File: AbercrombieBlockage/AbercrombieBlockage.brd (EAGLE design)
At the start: 54 x 52 mm, 29 parts, among them U1 CY8CKIT-142, U2 DMN3135LVT, U3 DMN3135LVT, U4 DMN3135LVT, U5 M95M01, U6 LDK130M-R

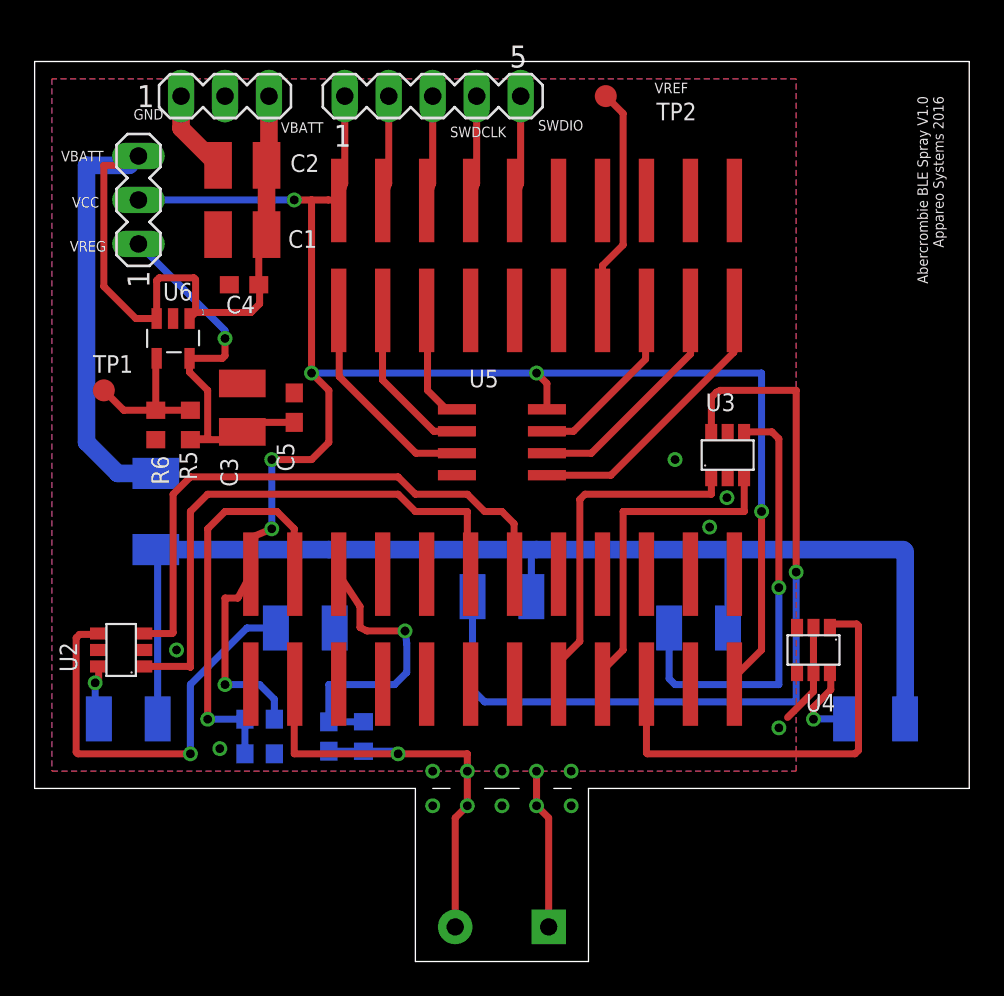
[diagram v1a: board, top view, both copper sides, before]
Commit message: Updated to fix issues with the layout.
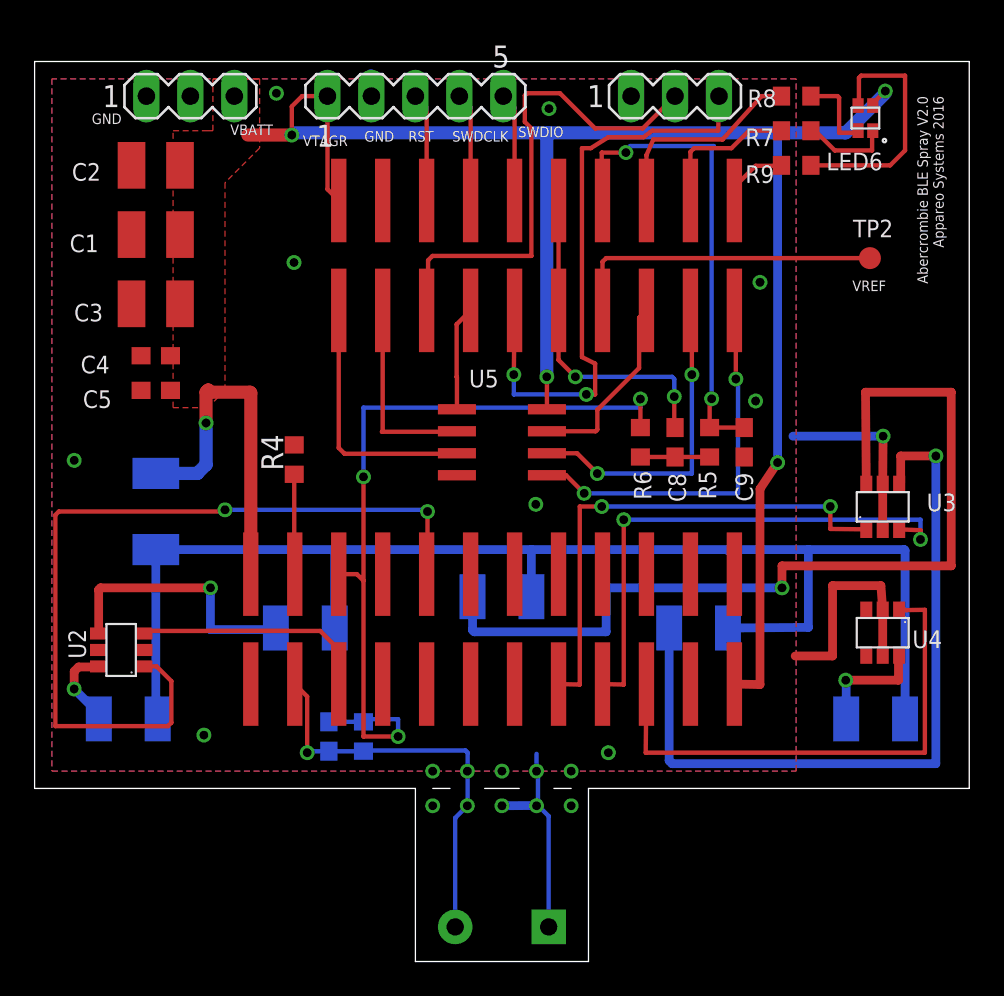
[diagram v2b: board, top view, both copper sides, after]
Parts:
- removed R3: DNP, resistor:R0603
- removed TP1: TPB1,27, testpad:B1,27
- removed U6: LDK130M-R, NicksParts:SOT23-5
- added C8: 20n, resistor:C0603
- added C9: 10n, resistor:C0603
- added LED6: LTST-C19HE1WT, NicksParts:LTST-C19HE1WT
- added R7: 200, resistor:R0603
- added R8, R9: 60, resistor:R0603
- R5, R6: value DNP -> 937.82k
- moved SV2 31.6 mm to (37.0, 50.0), turned to 0 degrees
- moved R5 30.0 mm to (39.0, 30.0)
- moved R6 28.0 mm to (35.0, 30.0)
- moved TP2 17.9 mm to (48.3, 40.6)
- moved R4 17.1 mm to (15.0, 29.0), flipped to the top, turned to 90 degrees
- moved U3 9.45 mm to (49.0, 26.3)
- moved C5 8.06 mm to (7.00, 33.0), turned to 180 degrees
- moved C3 7.81 mm to (7.00, 38.0), turned to 180 degrees
- moved C4 6.54 mm to (7.00, 35.0)
- moved C1 5.00 mm to (7.00, 42.0)
- moved C2 5.00 mm to (7.00, 46.0)
- moved U4 4.12 mm to (49.0, 19.0)
- moved SV1 2.00 mm to (9.00, 50.0)
- moved SV3 1.00 mm to (22.0, 50.0)
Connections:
- removed net VBATT: C1.1, C2.1, C4.1, R1.2, SV1.3, SV2.3, U6.1, U6.3
- new net BLUE: R9.2, U1.0.1
- new net GREEN: R8.2, U1.0.5
- new net N$11: LED6.GREEN, R8.1
- new net N$13: LED6.BLUE, R9.1
- new net OPAMP2+: C9.2, R5.2, U1.1
- new net OPAMP2_OUT: C8.1, U1.1.1, U1.1.2
- new net RED: R7.2, U1.0.3
- new net UART_RX: SV2.3, U1.1.4
- new net UART_TX: SV2.2, U1.1.5
- net CS: now also U1.1.3; no longer U1.1.5
- net GND: now also C9.1, SV2.1; no longer R6.2, U6.2
- net LED1: now also U1.2.6; no longer U1.4.1
- net LED2: now also U1.2.3; no longer U1.4.0
- net N$10: now also LED6.RED, R7.1; no longer R5.2, R6.1, TP1.TP, U6.4
- net N$7: now also C8.2, R6.2; no longer C3.1, C5.1, SV2.1, U6.5
- net OPAMP+: no longer R3.2
- net OPAMP_OUT: now also R6.1
- net VCC: now also C1.1, C2.1, C3.1, C4.1, C5.1, LED6.A, R1.2, SV1.3; no longer R3.1, SV2.2
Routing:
- net VBATT: track 60.1 -> 0.00 mm
- net UART_RX: track 0.00 -> 34.6 mm, vias 0 -> 2
- net UART_TX: track 0.00 -> 28.8 mm
- net OPAMP_OUT: track 17.4 -> 45.8 mm, vias 1 -> 3
- net OPAMP2+: track 0.00 -> 27.8 mm, vias 0 -> 2
- net LED2: track 35.1 -> 13.8 mm
- net OPAMP2_OUT: track 0.00 -> 19.2 mm, vias 0 -> 2
- net N$7: track 23.2 -> 4.00 mm, vias 1 -> 0
- net OPAMP+: track 24.8 -> 5.78 mm, vias 1 -> 0
- net N$5: track 25.8 -> 44.6 mm
- net VCC: track 101.8 -> 119.7 mm, vias 7 -> 5
- net LED1: track 33.1 -> 48.6 mm, vias 0 -> 2
- net N$13: track 0.00 -> 14.5 mm
- net GREEN: track 0.00 -> 12.1 mm
- net LED4: track 19.4 -> 30.8 mm, vias 0 -> 2
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- added copper zone on layer 1, net VCC
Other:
- board text added: "Abercrombie BLE Spray V2.0 Appareo Systems 2016"
- board text added: "RST"
- board text added: "VTAGR"
- board text removed: "Abercrombie BLE Spray V1.0 Appareo Systems 2016"
- board text removed: "VCC"
- board text removed: "VREG"

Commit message: Updated Abercrombie values.
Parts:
- C1: value 100u -> 220u
- C2: value 1u -> 220u
- C8: value 20n -> 0
- C9: value 10n -> 620K
- R5: value 937.82k -> 1M
- R6: value 937.82k -> DNP
- R7: value 200 -> 360
- R8, R9: value 60 -> 360
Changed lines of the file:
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@@
 <grid distance="0.05" unitdist="inch" unit="inch" style="lines" multiple="1" display="yes" altdistance="0.005" altunitdist="inch" altunit="inch"/>
 <layers>
-<layer number="1" name="Top" color="4" fill="1" visible="yes" active="yes"/>
+<layer number="1" name="Top" color="4" fill="1" visible="no" active="yes"/>
 <layer number="16" name="Bottom" color="1" fill="1" visible="yes" active="yes"/>
-<layer number="17" name="Pads" color="2" fill="1" visible="yes" active="yes"/>
-<layer number="18" name="Vias" color="2" fill="1" visible="yes" active="yes"/>
-<layer number="19" name="Unrouted" color="6" fill="1" visible="yes" active="yes"/>
-<layer number="20" name="Dimension" color="15" fill="1" visible="yes" active="yes"/>
-<layer number="21" name="tPlace" color="16" fill="1" visible="yes" active="yes"/>
-<layer number="22" name="bPlace" color="14" fill="1" visible="yes" active="yes"/>
-<layer number="23" name="tOrigins" color="15" fill="1" visible="yes" active="yes"/>
-<layer number="24" name="bOrigins" color="15" fill="1" visible="yes" active="yes"/>
+<layer number="17" name="Pads" color="2" fill="1" visible="no" active="yes"/>
+<layer number="18" name="Vias" color="2" fill="1" visible="no" active="yes"/>
+<layer number="19" name="Unrouted" color="6" fill="1" visible="no" active="yes"/>
+<layer number="20" name="Dimension" color="15" fill="1" visible="no" active="yes"/>
+<layer number="21" name="tPlace" color="16" fill="1" visible="no" active="yes"/>
+<layer number="22" name="bPlace" color="14" fill="1" visible="no" active="yes"/>
+<layer number="23" name="tOrigins" color="15" fill="1" visible="no" active="yes"/>
+<layer number="24" name="bOrigins" color="15" fill="1" visible="no" active="yes"/>
 <layer number="25" name="tNames" color="7" fill="1" visible="no" active="yes"/>
 <layer number="26" name="bNames" color="7" fill="1" visible="no" active="yes"/>
@@
 <layer number="43" name="vRestrict" color="2" fill="10" visible="no" active="yes"/>
 <layer number="44" name="Drills" color="7" fill="1" visible="no" active="yes"/>
-<layer number="45" name="Holes" color="7" fill="1" visible="yes" active="yes"/>
+<layer number="45" name="Holes" color="7" fill="1" visible="no" active="yes"/>
 <layer number="46" name="Milling" color="3" fill="1" visible="no" active="yes"/>
 <layer number="47" name="Measures" color="7" fill="1" visible="no" active="yes"/>
 <layer number="48" name="Document" color="7" fill="1" visible="no" active="yes"/>
 <layer number="49" name="Reference" color="7" fill="1" visible="no" active="yes"/>
-<layer number="51" name="tDocu" color="6" fill="1" visible="yes" active="yes"/>
+<layer number="51" name="tDocu" color="6" fill="1" visible="no" active="yes"/>
 <layer number="52" name="bDocu" color="7" fill="1" visible="no" active="yes"/>
 <layer number="90" name="Modules" color="5" fill="1" visible="no" active="no"/>
@@
 </autorouter>
 <elements>
-<element name="C1" library="resistor" package="C1210" value="100u" x="7" y="42" smashed="yes" rot="R180">
+<element name="C1" library="resistor" package="C1210" value="220u" x="7" y="42" smashed="yes" rot="R180">
 <attribute name="NAME" x="3.698" y="42" size="1.016" layer="25" rot="R180"/>
 <attribute name="VALUE" x="9.905" y="39.175" size="1.27" layer="27" rot="R180"/>
 </element>
-<element name="C2" library="resistor" package="C1210" value="1u" x="7" y="46" smashed="yes" rot="R180">
+<element name="C2" library="resistor" package="C1210" value="220u" x="7" y="46" smashed="yes" rot="R180">
 <attribute name="NAME" x="3.825" y="46.127" size="1.016" layer="25" rot="R180"/>
 <attribute name="VALUE" x="8.905" y="49.175" size="1.27" layer="27" rot="R180"/>
@@
 <attribute name="NAME" x="49" y="46.73" size="1.016" layer="25" rot="R180"/>
 </element>
-<element name="C8" library="resistor" package="C0603" value="20n" x="37" y="30" smashed="yes" rot="R270">
+<element name="C8" library="resistor" package="C0603" value="0" x="37" y="30" smashed="yes" rot="R270">
 <attribute name="NAME" x="36.619" y="28.222" size="1.016" layer="25" rot="R270"/>
 <attribute name="VALUE" x="35.095" y="30.635" size="1.27" layer="27" rot="R270"/>
 </element>
-<element name="R5" library="resistor" package="R0603" value="937.82k" x="39" y="30" smashed="yes" rot="R90">
+<element name="R5" library="resistor" package="R0603" value="1M" x="39" y="30" smashed="yes" rot="R90">
 <attribute name="NAME" x="39.381" y="26.698" size="1.016" layer="25" rot="R90"/>
 <attribute name="VALUE" x="40.905" y="29.365" size="1.27" layer="27" rot="R90"/>
 </element>
-<element name="R6" library="resistor" package="R0603" value="937.82k" x="35" y="30" smashed="yes" rot="R270">
+<element name="R6" library="resistor" package="R0603" value="DNP" x="35" y="30" smashed="yes" rot="R270">
 <attribute name="NAME" x="34.619" y="28.349" size="1.016" layer="25" rot="R270"/>
 <attribute name="VALUE" x="33.095" y="30.635" size="1.27" layer="27" rot="R270"/>
 </element>
-<element name="C9" library="resistor" package="C0603" value="10n" x="41" y="30" smashed="yes" rot="R90">
+<element name="C9" library="resistor" package="C0603" value="620K" x="41" y="30" smashed="yes" rot="R90">
 <attribute name="NAME" x="41.508" y="26.571" size="1.016" layer="25" rot="R90"/>
 <attribute name="VALUE" x="42.905" y="29.365" size="1.27" layer="27" rot="R90"/>
 </element>
-<element name="R7" library="resistor" package="R0603" value="200" x="44" y="48" smashed="yes" rot="R180">
+<element name="R7" library="resistor" package="R0603" value="360" x="44" y="48" smashed="yes" rot="R180">
 <attribute name="NAME" x="42.73" y="48.127" size="1.016" layer="25" rot="R180"/>
 <attribute name="VALUE" x="44.635" y="49.905" size="1.27" layer="27" rot="R180"/>
 </element>
-<element name="R8" library="resistor" package="R0603" value="60" x="44" y="50" smashed="yes" rot="R180">
+<element name="R8" library="resistor" package="R0603" value="360" x="44" y="50" smashed="yes" rot="R180">
 <attribute name="NAME" x="42.857" y="50.381" size="1.016" layer="25" rot="R180"/>
 <attribute name="VALUE" x="44.635" y="51.905" size="1.27" layer="27" rot="R180"/>
 </element>
-<element name="R9" library="resistor" package="R0603" value="60" x="44" y="46" smashed="yes" rot="R180">
+<element name="R9" library="resistor" package="R0603" value="360" x="44" y="46" smashed="yes" rot="R180">
 <attribute name="NAME" x="42.73" y="46" size="1.016" layer="25" rot="R180"/>
 <attribute name="VALUE" x="44.635" y="47.905" size="1.27" layer="27" rot="R180"/>

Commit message: Added a readme indicated the Abercrombie projects have been moved.
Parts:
- R2: value 20k -> 1k
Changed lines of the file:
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@@
 <attribute name="DIGIKEY_50_OHM" value="541-2477-1-ND" x="7" y="26" size="1.778" layer="28" rot="MR90" display="off"/>
 </element>
-<element name="R2" library="resistor" package="R0603" value="20k" x="19" y="13" smashed="yes" rot="MR270">
+<element name="R2" library="resistor" package="R0603" value="1k" x="19" y="13" smashed="yes" rot="MR270">
 <attribute name="NAME" x="19.868" y="17.064" size="1.016" layer="26" rot="MR270"/>
 <attribute name="VALUE" x="20.905" y="13.635" size="1.27" layer="28" rot="MR270"/>
